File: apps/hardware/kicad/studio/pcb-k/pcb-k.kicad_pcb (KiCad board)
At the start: 2 copper layers, 0 parts

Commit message: feat(hardware): ubicación de componentes de PCB-K y footprint del Choc V2 corregido
- tools/place_pcb_k.py ubica las 46 piezas en coordenadas del enclosure (re-ejecutable):
  contorno, bujes de los EC11, pasos de los separadores, Choc, LEDs bajo cada tecla y anillo de NAV
  con sus caps entre LEDs.
- Footprint SW_Kailh_Choc_V2_1u espejado (guía en (5,-5.15), pin 2 en (-5,3.8), vista superior),
  verificado con un Choc real.
- pcb-k.kicad_dru: holgura al borde de 0.2 mm solo dentro de cada SK6812MINI-E (ventana del
  footprint); el resto de la placa sigue en 0.3 mm.
- DRC sin errores; queda el ruteo (107 conexiones).

Co-Authored-By: Claude Opus 5.5 <noreply@anthropic.com>
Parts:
- added C1: 100nF, Capacitor_SMD:C_0603_1608Metric, B.Cu at (143.5, 155.0)
- added C10: 100nF, Capacitor_SMD:C_0603_1608Metric, B.Cu at (127.0, 164.5)
- added C11: 100nF, Capacitor_SMD:C_0603_1608Metric, B.Cu at (130.5, 158.5)
- added C12: 100nF, Capacitor_SMD:C_0603_1608Metric, B.Cu at (136.5, 155.0)
- added C13: 100nF, Capacitor_SMD:C_0603_1608Metric, B.Cu at (103.0, 133.1)
- added C14: 100nF, Capacitor_SMD:C_0603_1608Metric, B.Cu at (123.0, 133.1)
- added C15: 100nF, Capacitor_SMD:C_0603_1608Metric, B.Cu at (143.0, 133.1)
- added C16: 100nF, Capacitor_SMD:C_0603_1608Metric, B.Cu at (163.0, 133.1)
- added C17: 100nF, Capacitor_SMD:C_0603_1608Metric, B.Cu at (103.0, 163.1)
- added C18: 100nF, Capacitor_SMD:C_0603_1608Metric, B.Cu at (163.0, 163.1)
- added C19: 47uF, Capacitor_SMD:C_1206_3216Metric, B.Cu at (150.0, 129.0)
- added C2: 100nF, Capacitor_SMD:C_0603_1608Metric, B.Cu at (149.5, 158.5)
- added C3: 100nF, Capacitor_SMD:C_0603_1608Metric, B.Cu at (153.0, 164.5)
- added C4: 100nF, Capacitor_SMD:C_0603_1608Metric, B.Cu at (153.0, 171.5)
- added C5: 100nF, Capacitor_SMD:C_0603_1608Metric, B.Cu at (149.5, 177.5)
- added C6: 100nF, Capacitor_SMD:C_0603_1608Metric, B.Cu at (143.5, 181.0)
- added C7: 100nF, Capacitor_SMD:C_0603_1608Metric, B.Cu at (136.5, 181.0)
- added C8: 100nF, Capacitor_SMD:C_0603_1608Metric, B.Cu at (130.5, 177.5)
- added C9: 100nF, Capacitor_SMD:C_0603_1608Metric, B.Cu at (127.0, 171.5)
- added D1: SK6812MINI-E, LED_SMD:LED_SK6812MINI-E_3.2x2.8mm_P1.5mm_ReverseMount, B.Cu at (140.0, 155.0)
- added D10: SK6812MINI-E, LED_SMD:LED_SK6812MINI-E_3.2x2.8mm_P1.5mm_ReverseMount, B.Cu at (127.0, 168.0)
- added D11: SK6812MINI-E, LED_SMD:LED_SK6812MINI-E_3.2x2.8mm_P1.5mm_ReverseMount, B.Cu at (128.7, 161.5)
- added D12: SK6812MINI-E, LED_SMD:LED_SK6812MINI-E_3.2x2.8mm_P1.5mm_ReverseMount, B.Cu at (133.5, 156.7)
- added D13: SK6812MINI-E, LED_SMD:LED_SK6812MINI-E_3.2x2.8mm_P1.5mm_ReverseMount, B.Cu at (110.0, 133.1)
- added D14: SK6812MINI-E, LED_SMD:LED_SK6812MINI-E_3.2x2.8mm_P1.5mm_ReverseMount, B.Cu at (130.0, 133.1)
- added D15: SK6812MINI-E, LED_SMD:LED_SK6812MINI-E_3.2x2.8mm_P1.5mm_ReverseMount, B.Cu at (150.0, 133.1)
- added D16: SK6812MINI-E, LED_SMD:LED_SK6812MINI-E_3.2x2.8mm_P1.5mm_ReverseMount, B.Cu at (170.0, 133.1)
- added D17: SK6812MINI-E, LED_SMD:LED_SK6812MINI-E_3.2x2.8mm_P1.5mm_ReverseMount, B.Cu at (110.0, 163.1)
- added D18: SK6812MINI-E, LED_SMD:LED_SK6812MINI-E_3.2x2.8mm_P1.5mm_ReverseMount, B.Cu at (170.0, 163.1)
- added D2: SK6812MINI-E, LED_SMD:LED_SK6812MINI-E_3.2x2.8mm_P1.5mm_ReverseMount, B.Cu at (146.5, 156.7)
- added D3: SK6812MINI-E, LED_SMD:LED_SK6812MINI-E_3.2x2.8mm_P1.5mm_ReverseMount, B.Cu at (151.3, 161.5)
- added D4: SK6812MINI-E, LED_SMD:LED_SK6812MINI-E_3.2x2.8mm_P1.5mm_ReverseMount, B.Cu at (153.0, 168.0)
- added D5: SK6812MINI-E, LED_SMD:LED_SK6812MINI-E_3.2x2.8mm_P1.5mm_ReverseMount, B.Cu at (151.3, 174.5)
- added D6: SK6812MINI-E, LED_SMD:LED_SK6812MINI-E_3.2x2.8mm_P1.5mm_ReverseMount, B.Cu at (146.5, 179.3)
- added D7: SK6812MINI-E, LED_SMD:LED_SK6812MINI-E_3.2x2.8mm_P1.5mm_ReverseMount, B.Cu at (140.0, 181.0)
- added D8: SK6812MINI-E, LED_SMD:LED_SK6812MINI-E_3.2x2.8mm_P1.5mm_ReverseMount, B.Cu at (133.5, 179.3)
- added D9: SK6812MINI-E, LED_SMD:LED_SK6812MINI-E_3.2x2.8mm_P1.5mm_ReverseMount, B.Cu at (128.7, 174.5)
- added J1: A PCB-A (JST-SH 10), Connector_JST:JST_SH_SM10B-SRSS-TB_1x10-1MP_P1.00mm_Horizontal, B.Cu at (140.0, 127.5)
- added SW1: B1 OSC/INSERT, studio:SW_Kailh_Choc_V2_1u, F.Cu at (110.0, 138.0)
- added SW2: B2 ENV/SEND, studio:SW_Kailh_Choc_V2_1u, F.Cu at (130.0, 138.0)
- added SW3: B3 LFO/MASTER, studio:SW_Kailh_Choc_V2_1u, F.Cu at (150.0, 138.0)
- added SW4: B4 PRESET/FAV, studio:SW_Kailh_Choc_V2_1u, F.Cu at (170.0, 138.0)
- added SW5: B5 MODE, studio:SW_Kailh_Choc_V2_1u, F.Cu at (110.0, 168.0)
- added SW6: B6 HOLD/SHIFT, studio:SW_Kailh_Choc_V2_1u, F.Cu at (170.0, 168.0)
- added TP1: LED_DIN, TestPoint:TestPoint_Pad_D1.0mm, B.Cu at (130.0, 129.0)
- added TP2: LED_DOUT, TestPoint:TestPoint_Pad_D1.0mm, B.Cu at (176.0, 177.0)
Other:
- board outline added: 156 x 62 mm

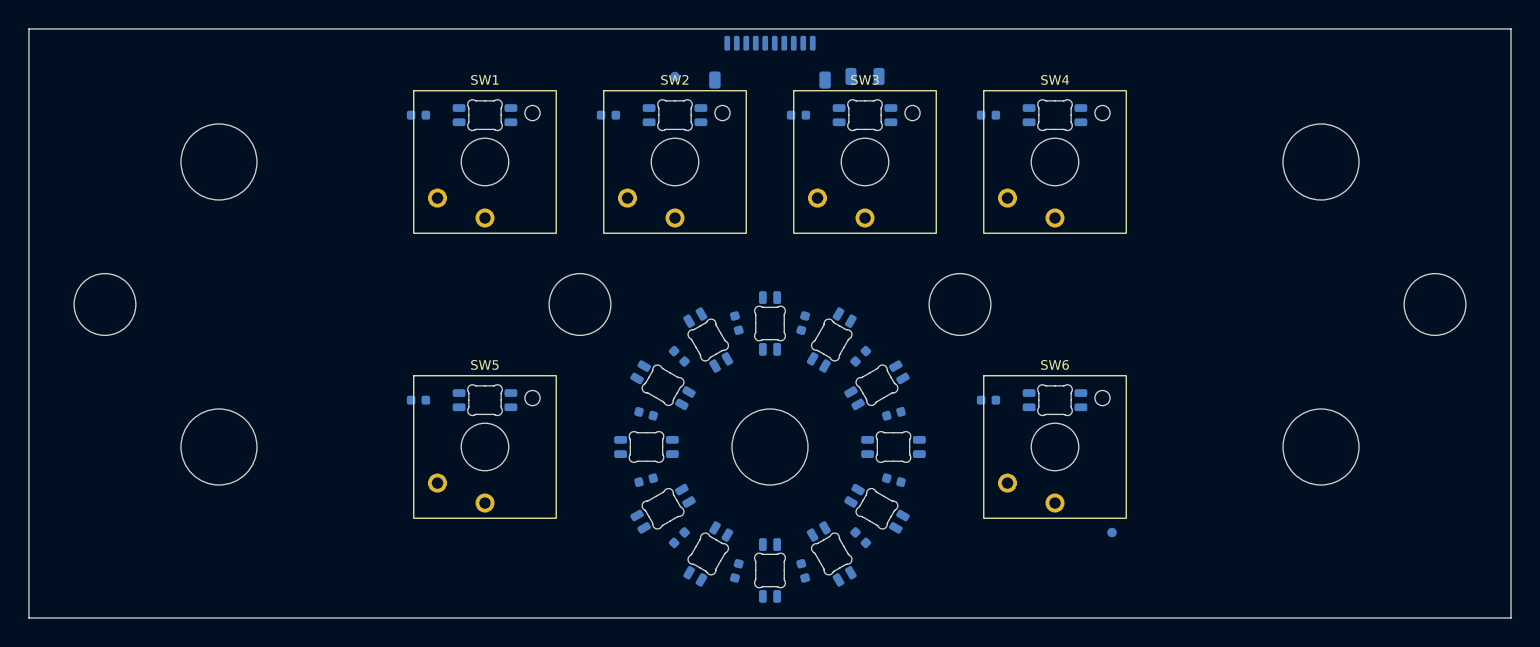
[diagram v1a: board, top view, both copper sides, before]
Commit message: feat(hardware): PCB-K ruteada (DRC limpio contra reglas de JLCPCB)
- Anillo de NAV: LEDs rotados 180° para que DOUT y DIN queden enfrentados en cada hueco (mismo
  orden e índices 0–11). Ruteo regular por script: anillo interior de +5V, saltos de datos por F.Cu
  que esquivan las ventanas de luz, una vía de GND por hueco (tools/route_pcb_k_ring.py).
- Zona de teclas con rutas explícitas (tools/route_pcb_k_keys.py): botones por F.Cu desde J1,
  cadena de datos y buses de +5V por B.Cu; capacitores de tecla a la derecha de cada LED; C19 sobre
  el bus de +5V; TP1/TP2 sobre sus pistas y fuera del BOM.
- Orden de pines de J1 nuevo en PCB-K y PCB-A (cable 1:1): B4, B6, B3, GND, +5V, GND, LED_DIN, B2,
  B5, B1. Evita ~14 cruces entre capas; los pines de la Teensy no cambian (02-studio-pcb.md §6.1).
- Planos de GND en F.Cu y B.Cu con costura cada 6 mm (tools/add_gnd_pours.py).
- Reglas de JLCPCB 2 capas en los tres proyectos: agujero-agujero 0.5 mm, vía ≥ 0.5/0.3, anillo
  ≥ 0.13; borde 0.25 mm (0.2 solo dentro de cada SK6812MINI-E).
- DRC con paridad de esquemático: 0 violaciones, 0 pads sin conectar, 0 errores de footprint.
- tools/route_board.py (Freerouting) queda como herramienta; no se usó en el resultado final.

Co-Authored-By: Claude Opus 5.5 <noreply@anthropic.com>
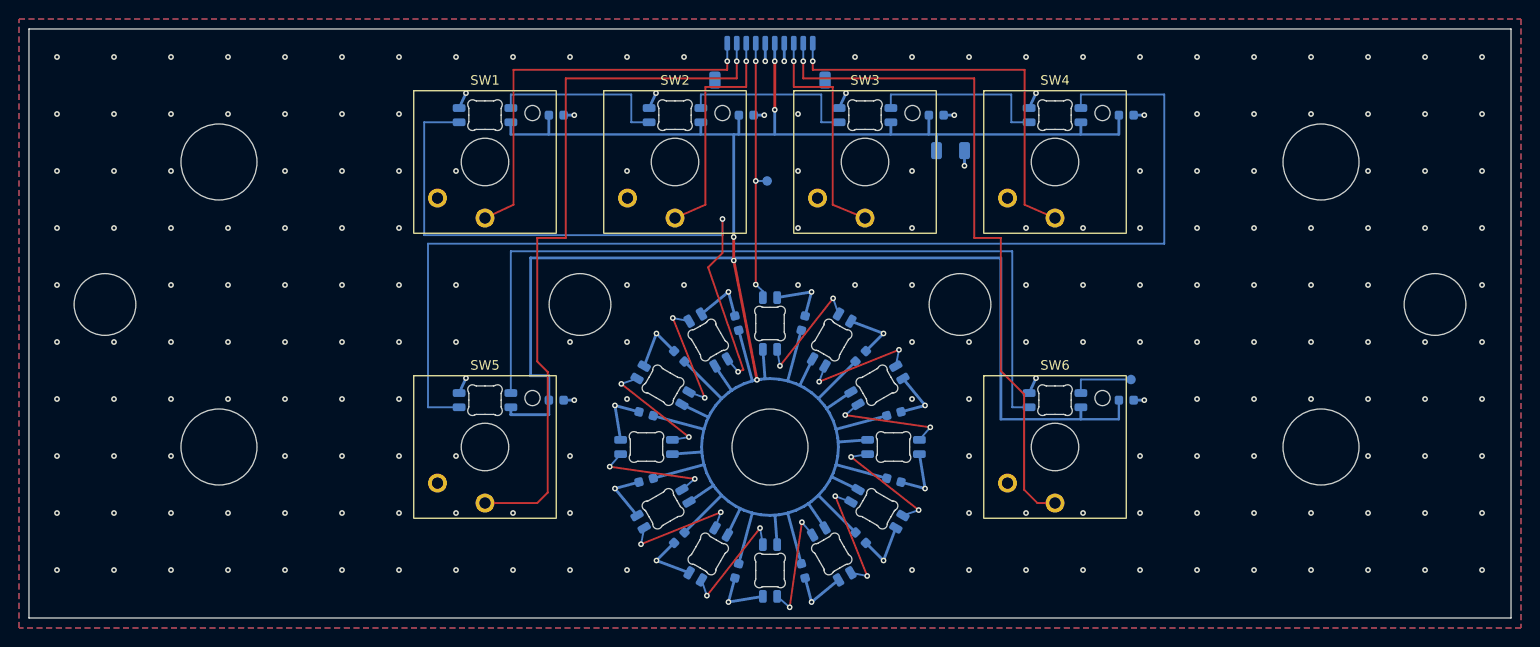
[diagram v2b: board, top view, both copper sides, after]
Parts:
- moved TP2 16.2 mm to (178.0, 160.9)
- moved TP1 14.7 mm to (139.7, 140.0)
- moved C13 14.5 mm to (117.5, 133.1)
- moved C14 14.5 mm to (137.5, 133.1)
- moved C15 14.5 mm to (157.5, 133.1)
- moved C16 14.5 mm to (177.5, 133.1)
- moved C17 14.5 mm to (117.5, 163.1)
- moved C18 14.5 mm to (177.5, 163.1)
- moved C19 11.9 mm to (159.0, 136.8)
- turned D1 to -90 degrees
- turned D10 to 0 degrees
- turned D11 to -30 degrees
- turned D12 to -60 degrees
- turned D2 to -120 degrees
- turned D3 to -150 degrees
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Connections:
- J1 pad 1: /+5V -> /B4
- J1 pad 10: /B6 -> /B1
- J1 pad 2: /GND -> /B6
- J1 pad 3: /LED_DIN -> /B3
- J1 pad 5: /B1 -> /+5V
- J1 pad 6: /B2 -> /GND
- J1 pad 7: /B3 -> /LED_DIN
- J1 pad 8: /B4 -> /B2
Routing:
- net /+5V: track 0.00 -> 369.0 mm, vias 0 -> 5
- net /LED_16: track 0.00 -> 123.9 mm
- net /GND: track 0.00 -> 98.1 mm, vias 0 -> 213
- net /LED_17: track 0.00 -> 85.9 mm
- net /B5: track 0.00 -> 75.8 mm, vias 0 -> 1
- net /B6: track 0.00 -> 72.6 mm, vias 0 -> 1
- net /LED_12: track 0.00 -> 68.1 mm, vias 0 -> 2
- net /B1: track 0.00 -> 42.8 mm, vias 0 -> 1
- net /B4: track 0.00 -> 42.8 mm, vias 0 -> 1
- net /LED_DIN: track 0.00 -> 28.3 mm, vias 0 -> 3
- net /B2: track 0.00 -> 24.8 mm, vias 0 -> 1
- net /B3: track 0.00 -> 24.8 mm, vias 0 -> 1
- net /LED_15: track 0.00 -> 18.9 mm
- net /LED_14: track 0.00 -> 18.9 mm
- net /LED_13: track 0.00 -> 18.9 mm
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- added copper zone on B.Cu, net /GND
- added copper zone on F.Cu, net /GND

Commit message: feat(hardware): archivos de fabricación JLCPCB y shield corregido en la portadora
- Portadora: las filas del Audio Shield estaban al revés (quedaba espejado respecto de la Teensy con el
  shield boca arriba). J16 (GND/0–12) pasa atrás y J15 adelante; re-ruteada, DRC con paridad 0/0/0.
- Números LCSC en los tres esquemáticos (set_lcsc.py), todo en ensamble Economic. PCB-K pasa al
  SK6812MINI-EA (mismo pinout y cuerpo, sin la restricción Standard-only del MINI-E).
- Escalera del PAD y acople al codec con valores Basic (33k/12k/5.1k, 4.7 µF): la simulación sigue
  pasando C1–C6 (tercera corrida en theory/03).
- export_fab.py: Gerbers + taladros, BOM y CPL en formato JLC; los THT usan el centro de sus pads y los
  IDC la rotación del modelo de JLC. Portadora con jacks e IDC ensamblados; el resto de los THT en
  fab/lcsc-piezas-sueltas.csv.
- sync_fp_fields.py también copia Value y LCSC a las placas.
- theory/02 §10C–10D: fabricación, montaje del shield, J9, J3 (USB host), corriente de la Pi y la
  verificación de punta a punta de las conexiones.

Co-Authored-By: Claude Opus 5.5 <noreply@anthropic.com>
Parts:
- D1, D10, D11, D12, D13, D14, D15, D16, D17, D18, D2, D3, D4, D5, D6, D7, D8, D9: value SK6812MINI-E -> SK6812MINI-EA

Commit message: feat(studio): vuelve PCB-K con los LEDs ensamblados (ADR-004 rev. 4)
El pedido se junta con GroovePush: tres placas como en el presupuesto original. La cadena de
PCB-K (anillo D1–D12, teclas D13–D18 = B1…B6) coincide con panel_leds, sin cambios de
firmware. Agujeros de los separadores Ø6.5 → Ø7.0 (hexagonal M3 de 5.5 mm); DRC 0.
Compras: Choc soldados a PCB-K, cable JST-SH ↔ header, terminales con ficha, amarres.

Co-Authored-By: Claude Opus 5.5 <noreply@anthropic.com>
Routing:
- net /GND: vias 213 -> 209
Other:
- outline, holes or cut-outs redrawn
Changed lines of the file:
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@@
 	(gr_circle
 		(center 70 153)
-		(end 73.25 153)
+		(end 73.5 153)
 		(stroke
 			(width 0.1)
@@
 	(gr_circle
 		(center 120 153)
-		(end 123.25 153)
+		(end 123.5 153)
 		(stroke
 			(width 0.1)
@@
 	(gr_circle
 		(center 160 153)
-		(end 163.25 153)
+		(end 163.5 153)
 		(stroke
 			(width 0.1)
@@
 	(gr_circle
 		(center 210 153)
-		(end 213.25 153)
+		(end 213.5 153)
 		(stroke
 			(width 0.1)
@@
 	)
 	(via
-		(at 70.95 156.95)
-		(size 0.6)
-		(drill 0.3)
-		(layers "F.Cu" "B.Cu")
-		(net "/GND")
-	)
-	(via
 		(at 70.95 162.95)
 		(size 0.6)
@@
 	)
 	(via
-		(at 160.95 156.95)
-		(size 0.6)
-		(drill 0.3)
-		(layers "F.Cu" "B.Cu")
-		(net "/GND")
-	)
-	(via
 		(at 64.95 150.95)
 		(size 0.6)
@@
 	)
 	(via
-		(at 208.95 156.95)
-		(size 0.6)
-		(drill 0.3)
-		(layers "F.Cu" "B.Cu")
-		(net "/GND")
-	)
-	(via
 		(at 208.95 162.95)
 		(size 0.6)
@@
 	)
 	(via
-		(at 118.95 156.95)
-		(size 0.6)
-		(drill 0.3)
-		(layers "F.Cu" "B.Cu")
-		(net "/GND")
-	)
-	(via
 		(at 151.950104 179.950104)
 		(size 0.6)
@@
 			"5ab4bb8c-ccc4-4144-9568-4c1f5e19bfe0" "5dc61dea-fa7c-405b-bc10-3345c18acbca"
 			"5dd6950f-0c48-4c22-8d68-0194b6ba7a54" "5f87d1e9-7a3d-41fd-b4c9-705294de49fe"
-			"60b8e96e-bd98-43e0-b1c7-21f60683a20b" "622e10c1-1446-4c8f-b5df-655e28486c46"
-			"64c91895-c12b-4b72-81ea-b9cdceb3b2f7" "659582f1-1545-4754-a6a5-63f7bb3214f9"
-			"66e97ab8-f9f1-4eef-8dba-ed2b03b2fb91" "685c2c4e-7cf1-4f80-be10-a8a2951fd086"
-			"6ade69dc-31bb-46e2-b014-71842b0db01a" "6b132e91-cb21-406b-acab-55ba4ff999de"
-			"6b917011-7ef3-4b17-aae2-5ef32e62aa6a" "6bb19bab-ee9a-4675-86d7-0dc862da1cac"
-			"6ce20356-6d05-475f-8146-f337abb18559" "6d79a937-787e-4076-a090-eebbb423be58"
-			"6e467a11-77a3-44b9-b263-984667dc9b4e" "6e91f887-2fd5-47d5-b68e-e382d56083b9"
-			"6f27940a-e449-438d-ae12-52106f6896be" "6f4328fc-365f-4190-b9a8-a323bf345b7f"
-			"6f4b3636-36ec-478c-957f-b9cfce767932" "6fa737d1-fe92-465b-b4e8-4fc121d6797a"
-			"7034106e-d7a9-4fe0-9392-d9c9a8559f21" "72095bf3-0f86-4115-a93c-b8d1f018b08d"
-			"78a7099e-2b01-4a53-a24d-24cbb81e5c2a" "7c578c28-8fc8-410e-a217-084b46a2b9a3"
-			"7ca24f01-ffb6-444a-9ea7-27c6673e019c" "7d1b517f-b5b2-457e-9bc2-f4aaffab1a45"
-			"7d4af1b6-1442-424f-80fe-58e89e3f4b11" "7d8ed7eb-ecf8-40e3-927f-843097e59c4a"
-			"7ef96a3a-4c7e-49ce-85d8-fc661923db5d" "7f318ecb-7f90-457c-b924-f96c13063b95"
-			"819dc836-ccbc-47ea-b2df-98e8308c252b" "830f9ce3-ce21-4565-8a06-78b065906136"
+			"622e10c1-1446-4c8f-b5df-655e28486c46" "64c91895-c12b-4b72-81ea-b9cdceb3b2f7"
+			"659582f1-1545-4754-a6a5-63f7bb3214f9" "66e97ab8-f9f1-4eef-8dba-ed2b03b2fb91"
+			"685c2c4e-7cf1-4f80-be10-a8a2951fd086" "6ade69dc-31bb-46e2-b014-71842b0db01a"
+			"6b132e91-cb21-406b-acab-55ba4ff999de" "6b917011-7ef3-4b17-aae2-5ef32e62aa6a"
+			"6bb19bab-ee9a-4675-86d7-0dc862da1cac" "6ce20356-6d05-475f-8146-f337abb18559"
+			"6d79a937-787e-4076-a090-eebbb423be58" "6e467a11-77a3-44b9-b263-984667dc9b4e"
+			"6e91f887-2fd5-47d5-b68e-e382d56083b9" "6f27940a-e449-438d-ae12-52106f6896be"
+			"6f4328fc-365f-4190-b9a8-a323bf345b7f" "6f4b3636-36ec-478c-957f-b9cfce767932"
+			"6fa737d1-fe92-465b-b4e8-4fc121d6797a" "7034106e-d7a9-4fe0-9392-d9c9a8559f21"
+			"72095bf3-0f86-4115-a93c-b8d1f018b08d" "78a7099e-2b01-4a53-a24d-24cbb81e5c2a"
+			"7c578c28-8fc8-410e-a217-084b46a2b9a3" "7ca24f01-ffb6-444a-9ea7-27c6673e019c"
+			"7d1b517f-b5b2-457e-9bc2-f4aaffab1a45" "7d4af1b6-1442-424f-80fe-58e89e3f4b11"
+			"7d8ed7eb-ecf8-40e3-927f-843097e59c4a" "7ef96a3a-4c7e-49ce-85d8-fc661923db5d"
+			"7f318ecb-7f90-457c-b924-f96c13063b95" "819dc836-ccbc-47ea-b2df-98e8308c252b"
 			"838a4121-2a9a-46fb-88d6-0dbf1096cbd9" "850cad0c-908c-427e-9eb7-a18e4a250d54"
 			"865b3f3e-6fda-4cdc-8e97-f784ee730b02" "86c06ea3-62cb-4658-89c7-53a03b7ca657"
@@
 			"a4820b4d-23c5-41fe-adaa-c46d87975670" "a70c3b3d-6de8-4cc3-ba24-1bf15b608b21"
 			"a7bc8fbf-ff2c-45f0-be15-b0f435a59984" "a97b6aca-59f8-47e5-a548-1e7473643a15"
-			"a9ce0504-bbdd-47ac-b09b-a7370e0b2df5" "aa6bf2c0-01c6-42b9-8adc-311d772bc17b"
-			"abf15420-ba8a-4d3b-8b85-fb4f819a110a" "ac80e31b-06cb-4e7b-8454-08c1592ce3a4"
-			"aeba4551-5538-4d69-a696-f7e9a6d20aa7" "b6ab2e63-09fa-4181-8d16-621b53c46062"
+			"a9ce0504-bbdd-47ac-b09b-a7370e0b2df5" "abf15420-ba8a-4d3b-8b85-fb4f819a110a"
+			"ac80e31b-06cb-4e7b-8454-08c1592ce3a4" "b6ab2e63-09fa-4181-8d16-621b53c46062"
 			"b793d130-cd11-4d70-acdb-24b017795255" "b8959975-f680-4d33-bd33-389dca988041"
 			"badcc586-2b61-4a72-bee6-0e2cb412c2a9" "bb10ca80-c5b0-4df2-a7f5-f53d23b02e84"
